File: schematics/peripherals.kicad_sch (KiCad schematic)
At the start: 4 parts

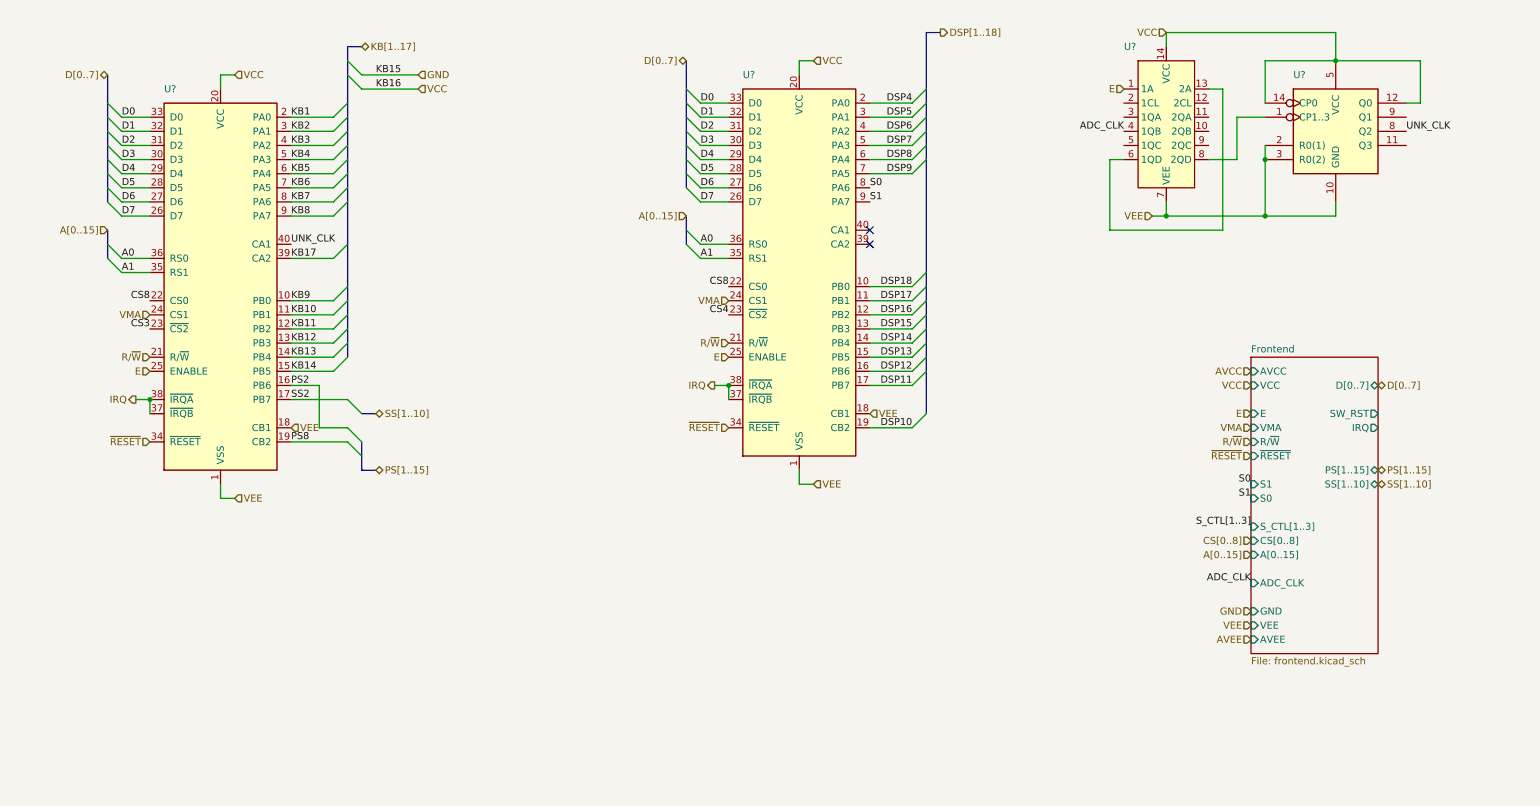
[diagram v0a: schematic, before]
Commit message: Moved more components into hierachical sheets, misc cleanup
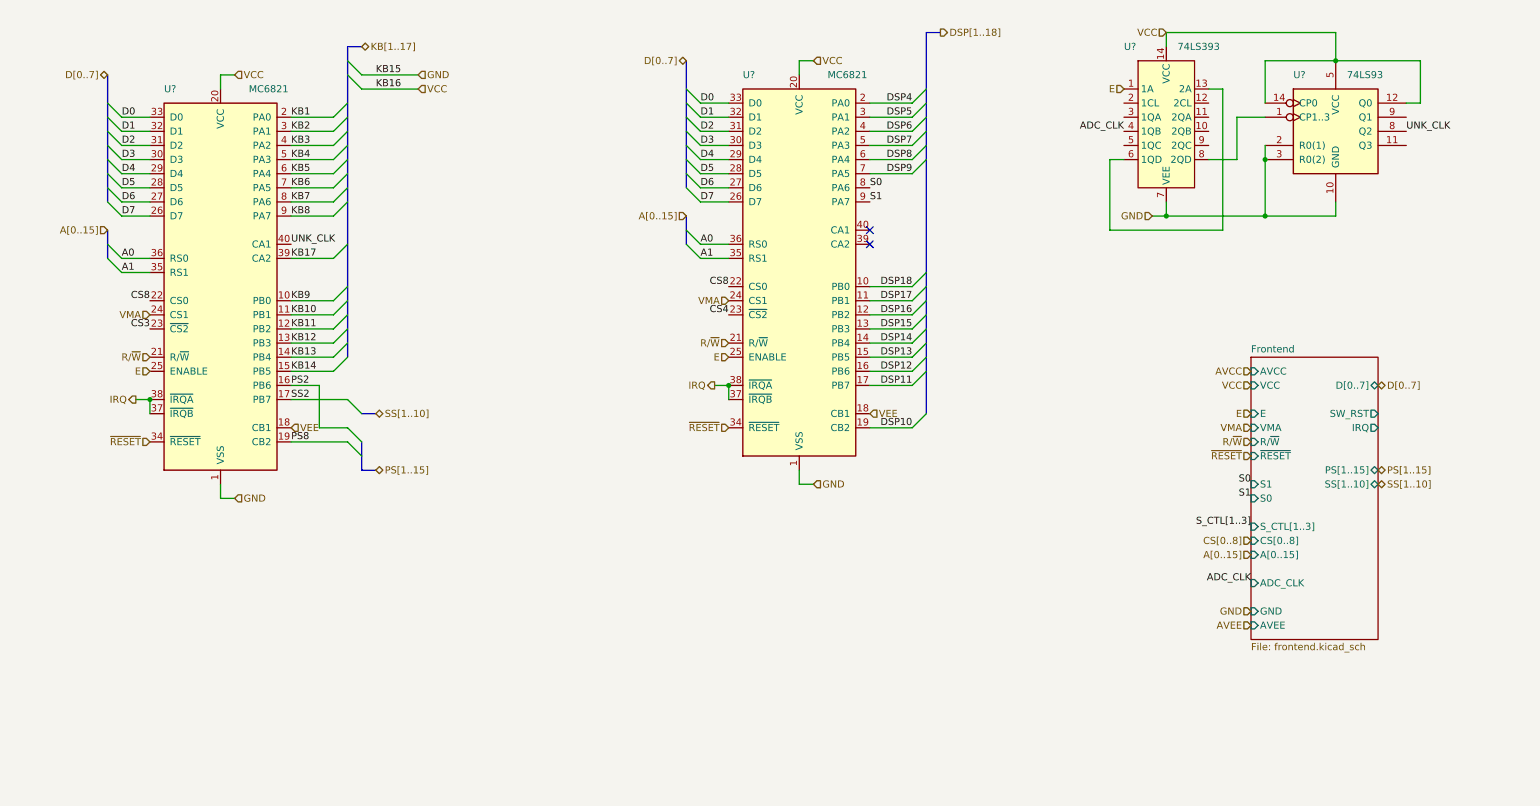
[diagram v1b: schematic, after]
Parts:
- U?: value ~ -> 74LS393
- U?: value ~ -> 74LS93
- U? (x2): value ~ -> MC6821
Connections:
- net GND: now also U?.1 (VSS), U?.1 (VSS), U?.10 (GND), U?.2 (R0(1)), U?.3 (R0(2)), U?.7 (VEE)
- net VEE: no longer U?.1 (VSS), U?.1 (VSS), U?.10 (GND), U?.2 (R0(1)), U?.3 (R0(2)), U?.7 (VEE)
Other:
- sheet Frontend ports: added none; removed VEE
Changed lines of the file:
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@@
     (effects (font (size 1.27 1.27)) (justify right bottom))
   )
-  (hierarchical_label "VEE" (shape input) (at 236.22 129.54 180)
-    (effects (font (size 1.27 1.27)) (justify right))
-  )
   (hierarchical_label "~{RESET}" (shape input) (at 38.1 96.52 180)
     (effects (font (size 1.27 1.27)) (justify right))
   )
-  (hierarchical_label "VEE" (shape input) (at 218.44 55.88 180)
-    (effects (font (size 1.27 1.27)) (justify right))
-  )
-  (hierarchical_label "VEE" (shape input) (at 157.48 104.14 0)
+  (hierarchical_label "GND" (shape input) (at 157.48 104.14 0)
     (effects (font (size 1.27 1.27)) (justify left))
   )
@@
     (effects (font (size 1.27 1.27)) (justify left))
   )
+  (hierarchical_label "GND" (shape input) (at 53.34 106.68 0)
+    (effects (font (size 1.27 1.27)) (justify left))
+  )
   (hierarchical_label "AVCC" (shape input) (at 236.22 83.82 180)
     (effects (font (size 1.27 1.27)) (justify right))
@@
     (effects (font (size 1.27 1.27)) (justify right))
   )
-  (hierarchical_label "VEE" (shape input) (at 53.34 106.68 0)
-    (effects (font (size 1.27 1.27)) (justify left))
-  )
   (hierarchical_label "D[0..7]" (shape bidirectional) (at 134.62 27.94 180)
     (effects (font (size 1.27 1.27)) (justify right))
@@
     (effects (font (size 1.27 1.27)) (justify right))
   )
-  (hierarchical_label "AVEE" (shape input) (at 236.22 132.08 180)
+  (hierarchical_label "AVEE" (shape input) (at 236.22 129.54 180)
     (effects (font (size 1.27 1.27)) (justify right))
   )
   (hierarchical_label "R{slash}~{W}" (shape input) (at 142.24 78.74 180)
+    (effects (font (size 1.27 1.27)) (justify right))
+  )
+  (hierarchical_label "GND" (shape input) (at 218.44 55.88 180)
     (effects (font (size 1.27 1.27)) (justify right))
   )
@@
       (effects (font (size 1.27 1.27)) (justify left))
     )
-    (property "Value" "~" (id 1) (at 222.9994 25.4 0)
+    (property "Value" "74LS393" (id 1) (at 222.9994 25.4 0)
       (effects (font (size 1.27 1.27)) (justify left))
     )
@@
       (effects (font (size 1.27 1.27)) (justify left))
     )
-    (property "Value" "~" (id 1) (at 253.4794 30.48 0)
+    (property "Value" "74LS93" (id 1) (at 253.4794 30.48 0)
       (effects (font (size 1.27 1.27)) (justify left))
     )
@@
       (effects (font (size 1.27 1.27)) (justify left))
     )
-    (property "Value" "~" (id 1) (at 160.02 30.48 0)
+    (property "Value" "MC6821" (id 1) (at 160.02 30.48 0)
       (effects (font (size 1.27 1.27)) (justify left))
     )
@@
       (effects (font (size 1.27 1.27)) (justify left))
     )
-    (property "Value" "~" (id 1) (at 55.88 33.02 0)
+    (property "Value" "MC6821" (id 1) (at 55.88 33.02 0)
       (effects (font (size 1.27 1.27)) (justify left))
     )
@@
     (pin "9")
   )
-  (sheet (at 236.22 81.28) (size 22.86 53.34) (fields_autoplaced)
+  (sheet (at 236.22 81.28) (size 22.86 50.8) (fields_autoplaced)
     (stroke (width 0.1524) (type solid) (color 0 0 0 0))
     (fill (color 0 0 0 0.0000))
@@
       (effects (font (size 1.27 1.27)) (justify left bottom))
     )
-    (property "Sheet file" "frontend.kicad_sch" (id 1) (at 236.22 135.2046 0)
+    (property "Sheet file" "frontend.kicad_sch" (id 1) (at 236.22 132.6646 0)
       (effects (font (size 1.27 1.27)) (justify left top))
     )
-    (pin "AVEE" input (at 236.22 132.08 180)
-      (effects (font (size 1.27 1.27)) (justify left))
-    )
-    (pin "VEE" input (at 236.22 129.54 180)
-      (effects (font (size 1.27 1.27)) (justify left))
-    )
+    (pin "AVEE" input (at 236.22 129.54 180)
+      (effects (font (size 1.27 1.27)) (justify left))
+    )

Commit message: cleanup, fixes, started on power supplies
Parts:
- added RP3: 4k7, Resistor_THT:R_Array_SIP9, symbol Device:R_Network08
- IC19, IC20: renamed from U?; footprint (none) -> Package_DIP:DIP-40_W15.24mm
- gave numbers to parts that had none: 2
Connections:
- net GND: no longer IC20.1 (VSS)
- net KB10: now also RP3.3 (R2)
- net KB11: now also RP3.4 (R3)
- net KB12: now also RP3.5 (R4)
- net KB13: now also RP3.6 (R5)
- net KB14: now also RP3.7 (R6)
- net KB9: now also RP3.2 (R1)
- net PS2: now also RP3.8 (R7)
- net SS2: now also RP3.9 (R8)
- net VCC: now also RP3.1 (common)
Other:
- sheet Frontend ports: added none; removed S_CTL[1..3]
- moved on the sheet: IC16, IC17, IC19

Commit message: More power supply work
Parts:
- IC16: value 74LS93 -> 74LD93
- IC17: value 74LS393 -> 74LD393
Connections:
- net S0 is gone; now on net D0: IC20.8 (PA6)
- net S1 is gone; now on net D1: IC20.9 (PA7)
- net GND: now also IC20.1 (VSS), IC20.18 (CB1)
- net VEE: no longer IC20.18 (CB1)
- net SS2 renamed DD2
